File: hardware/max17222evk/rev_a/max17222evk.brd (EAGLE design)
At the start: 160 x 100 mm, 20 parts, among them U1 MAX17222, U2 MAX17222

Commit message: added a first layout for one of the regulators
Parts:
- moved TP6 262.1 mm to (10.2, 25.4)
- moved TP5 236.7 mm to (10.2, 15.2)
- moved TP4 226.6 mm to (10.2, 20.3)
- moved TP3 201.2 mm to (10.2, 10.2)
- moved TP2 180.8 mm to (61.0, 10.2)
- moved TP1 139.8 mm to (53.3, 10.2)
- moved JP2 125.1 mm to (54.6, 19.8), turned to 90 degrees
- moved JP1 122.7 mm to (54.9, 37.3), turned to 90 degrees
- moved L1 87.0 mm to (35.8, 43.8)
- moved S1 84.4 mm to (22.9, 33.0), turned to 90 degrees
- moved S2 79.1 mm to (26.9, 15.2), turned to 90 degrees
- moved L2 77.2 mm to (35.6, 24.6), turned to 180 degrees
- moved R1 74.6 mm to (35.6, 35.1), turned to 90 degrees
- moved R2 63.4 mm to (35.6, 17.5), turned to 90 degrees
- moved C2 62.8 mm to (39.1, 35.1), turned to 270 degrees
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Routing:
- net N$7: track 0.00 -> 12.5 mm
- net IN2: track 0.00 -> 4.37 mm
- net N$12: track 0.00 -> 3.63 mm
- added copper zone on layer 1, net GND
- added copper zone on layer 16, net GND
- added copper zone on layer 1, net IN2
- added copper zone on layer 1, net SW2
- added copper zone on layer 1, net VOUT2

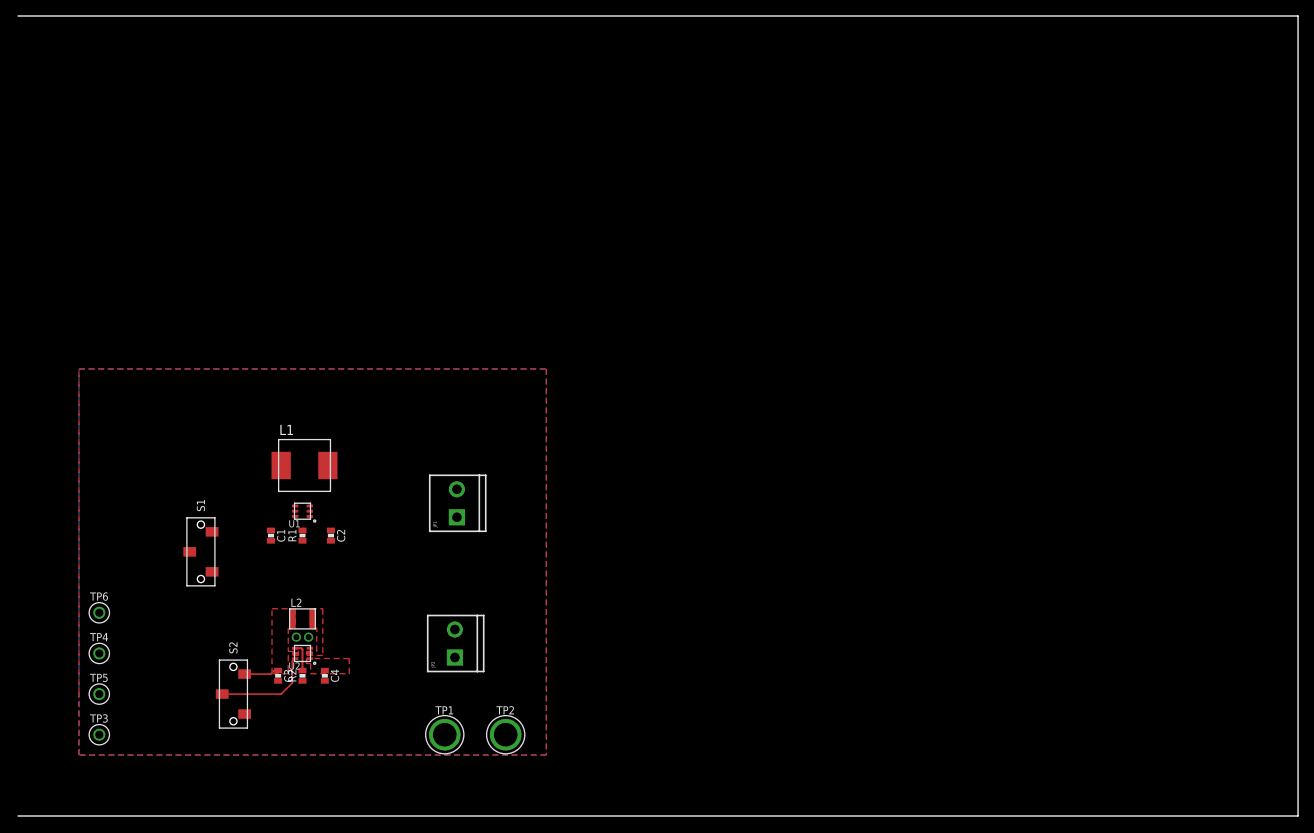
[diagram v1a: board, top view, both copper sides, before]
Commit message: routed board, flipped load screw terminals
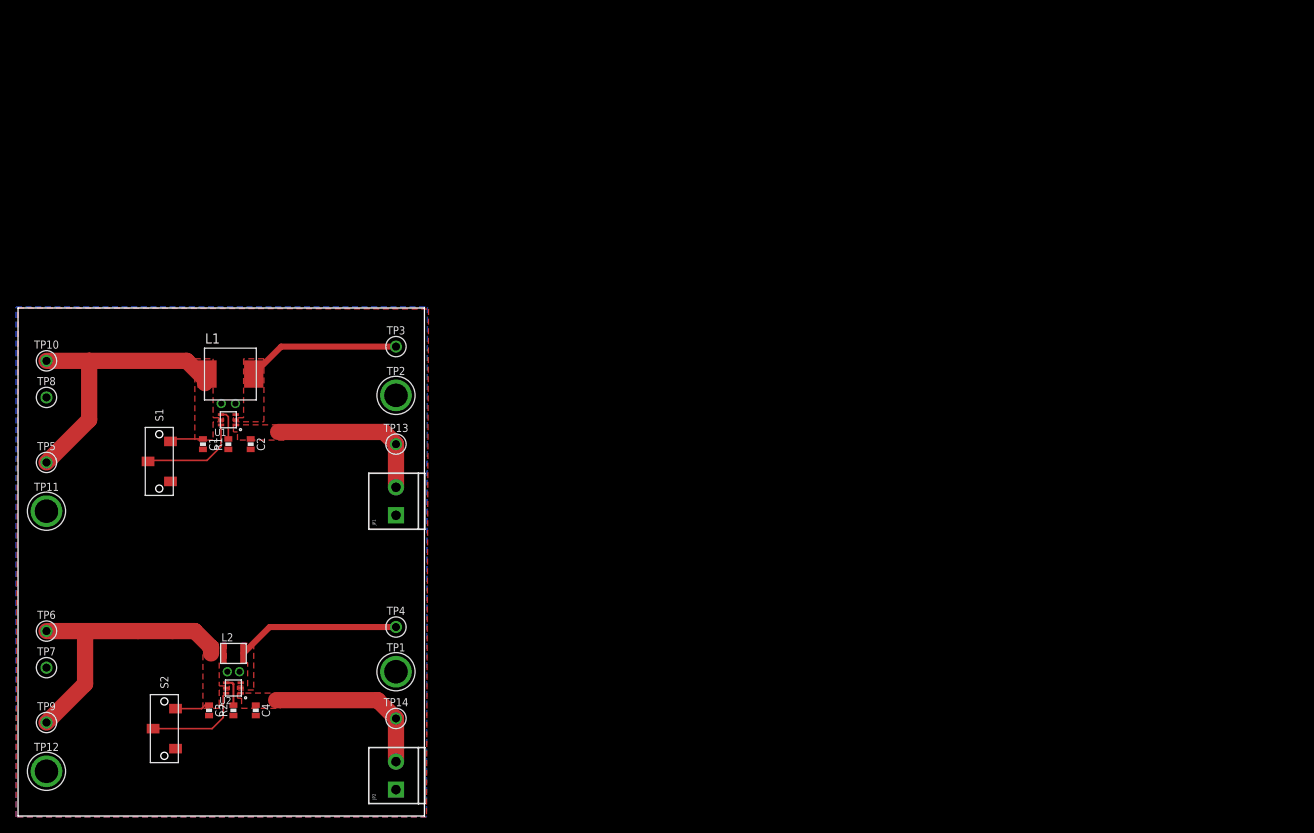
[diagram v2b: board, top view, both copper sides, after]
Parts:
- added TP10, TP13, TP14, TP7, TP8, TP9: TEST_POINT_0.040IN, headers:TESTPOINT_0.040IN
- added TP11, TP12: TEST_POINT_0.112IN, headers:TESTPOINT_0.112IN
- moved TP3 61.1 mm to (47.2, 58.7)
- moved TP2 44.6 mm to (47.2, 52.6)
- moved TP4 37.2 mm to (47.2, 23.6)
- moved TP5 29.7 mm to (3.56, 44.2)
- moved JP2 18.1 mm to (47.2, 3.30)
- moved C2 15.2 mm to (29.1, 46.5)
- moved L1 14.7 mm to (26.5, 55.2)
- moved R1 14.7 mm to (26.3, 46.5)
- moved U1 14.7 mm to (26.3, 49.5)
- moved C1 14.2 mm to (23.1, 46.5)
- moved S1 12.4 mm to (17.7, 44.3)
- moved TP1 9.96 mm to (47.2, 18.0)
- moved L2 9.66 mm to (26.9, 20.3)
- moved U2 9.66 mm to (26.9, 16.0)
- moved R2 9.66 mm to (26.9, 13.2)
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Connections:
- net GND: now also JP1.1, JP2.1, TP11.1, TP12.1, TP7.TESTPOINT, TP8.TESTPOINT; no longer JP1.2, JP2.2
- net IN1: now also TP10.TESTPOINT
- net IN2: now also TP9.TESTPOINT
- net VOUT1: now also JP1.2, TP13.TESTPOINT; no longer JP1.1
- net VOUT2: now also JP2.2, TP14.TESTPOINT; no longer JP2.1
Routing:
- net IN1: track 0.00 -> 40.4 mm
- net IN2: track 4.37 -> 40.0 mm
- net VOUT2: track 0.00 -> 21.3 mm
- net VOUT1: track 0.00 -> 20.8 mm
- net SW2: track 0.00 -> 20.5 mm
- net SW1: track 0.00 -> 19.2 mm
- net N$2: track 0.00 -> 12.6 mm
- net N$5: track 0.00 -> 3.81 mm
- added copper zone on layer 1, net IN1
- added copper zone on layer 1, net SW1
- added copper zone on layer 1, net VOUT1
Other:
- board size 160 x 100 mm -> 50.8 x 63.5 mm

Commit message: layout with silk
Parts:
- added U$1: (no value), logos:UCB_CAL_100MIL
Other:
- board text added: "DISABLE"
- board text added: "ENABLE"
- board text added: "GND"
- board text added: "Inductor Switch"
- board text added: "MAX17222 Evaluation Board Joshua Adkins - Rev A - 07/2017"
- board text added: "Regulator 1 - 3.3V - High Efficiency Inductor"
- board text added: "Regulator 2 - 3.3V - Small Inductor"
- board text added: "VIN"
- board text added: "VOUT"

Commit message: added resistor to enable line
I believe this is necessary for lower power operation.
It is in maxim's EVK
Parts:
- added R3, R4: 33M, passives:0603-RES
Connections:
- removed net N$7: S2.2, U2.6
- new net N$1: R3.2, S1.2
- new net N$3: R4.2, S2.2
- new net N$4: R4.1, U2.6
- net N$2: now also R3.1; no longer S1.2
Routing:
- net N$7: track 12.5 -> 0.00 mm
- net N$4: track 0.00 -> 7.33 mm
- net N$1: track 0.00 -> 6.43 mm
- net N$3: track 0.00 -> 6.36 mm
- net N$2: track 12.6 -> 7.28 mm

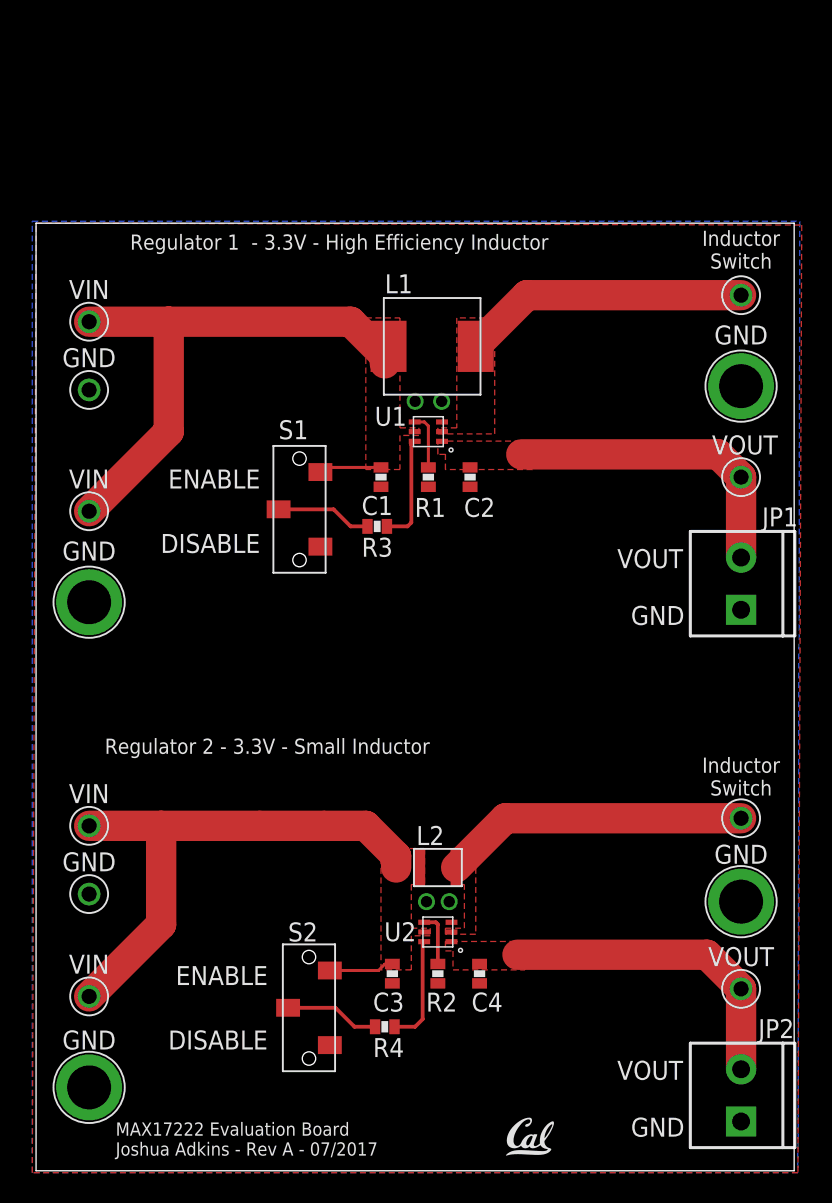
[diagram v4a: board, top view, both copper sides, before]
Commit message: added mounting holes, fixed switch
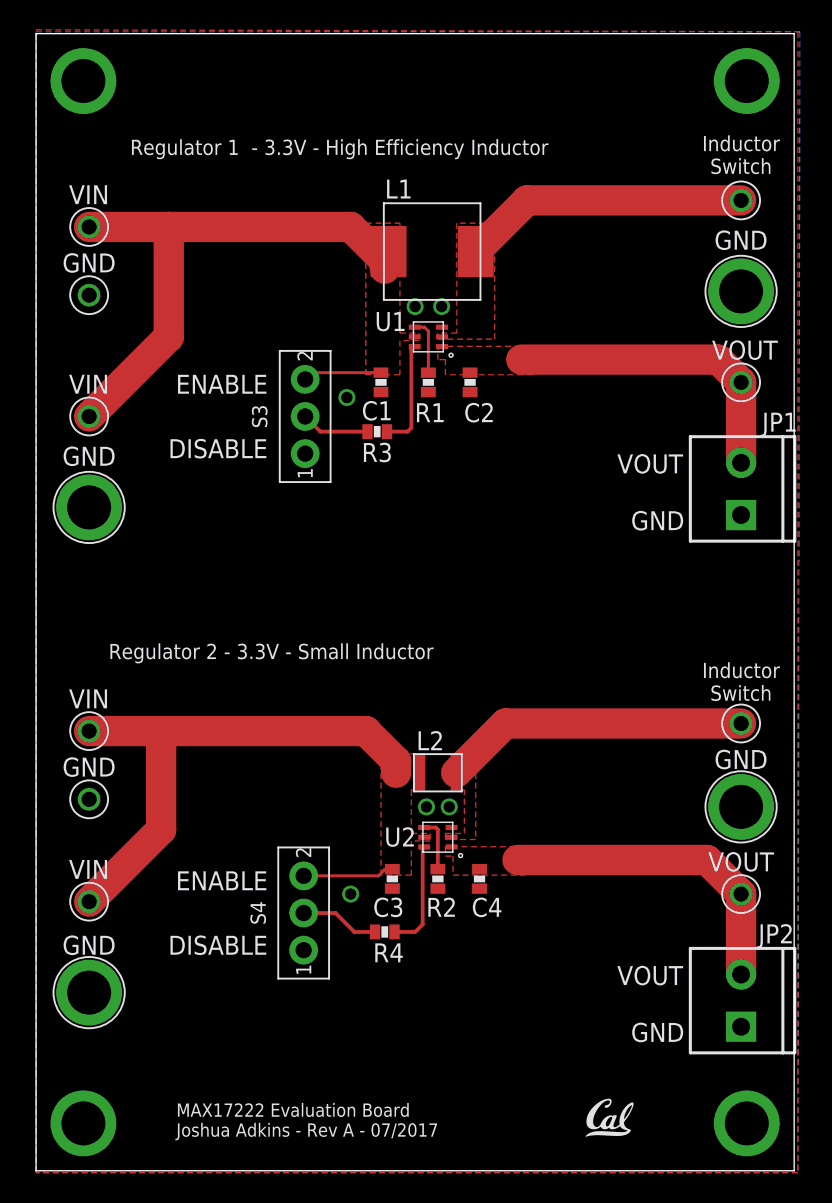
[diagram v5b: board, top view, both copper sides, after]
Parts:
- removed S1, S2: CL-SB-12X, switches:CL-SB-12A
- added S3, S4: TE_SSA12/SPDT, switches:TE_SSA12/SPDT
- moved C1 6.35 mm to (23.1, 52.8)
- moved C2 6.35 mm to (29.1, 52.8)
- moved JP1 6.35 mm to (47.2, 43.9)
- moved L1 6.35 mm to (26.5, 61.6)
- moved L2 6.35 mm to (26.9, 26.7)
- moved R1 6.35 mm to (26.3, 52.8)
- moved R3 6.35 mm to (22.9, 49.5)
- moved TP1 6.35 mm to (47.2, 24.4)
- moved TP10 6.35 mm to (3.56, 63.2)
- moved TP11 6.35 mm to (3.56, 44.5)
- moved TP13 6.35 mm to (47.2, 52.8)
- moved TP14 6.35 mm to (47.2, 18.5)
- moved TP3 6.35 mm to (47.2, 65.0)
- moved TP4 6.35 mm to (47.2, 30.0)
- moved TP5 6.35 mm to (3.56, 50.5)
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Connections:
- net GND: now also S3.1, S4.1; no longer S1.1, S2.1
- net IN1: now also S3.2; no longer S1.3
- net IN2: now also S4.2; no longer S2.3
- net N$1: now also S3.IN; no longer S1.2
- net N$3: now also S4.IN; no longer S2.2
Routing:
- net N$1: track 6.43 -> 4.60 mm
- net IN2: track 40.0 -> 41.7 mm
- net IN1: track 40.4 -> 41.4 mm
- net N$3: track 6.36 -> 5.31 mm
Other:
- board size 50.8 x 63.5 mm -> 50.8 x 76.2 mm

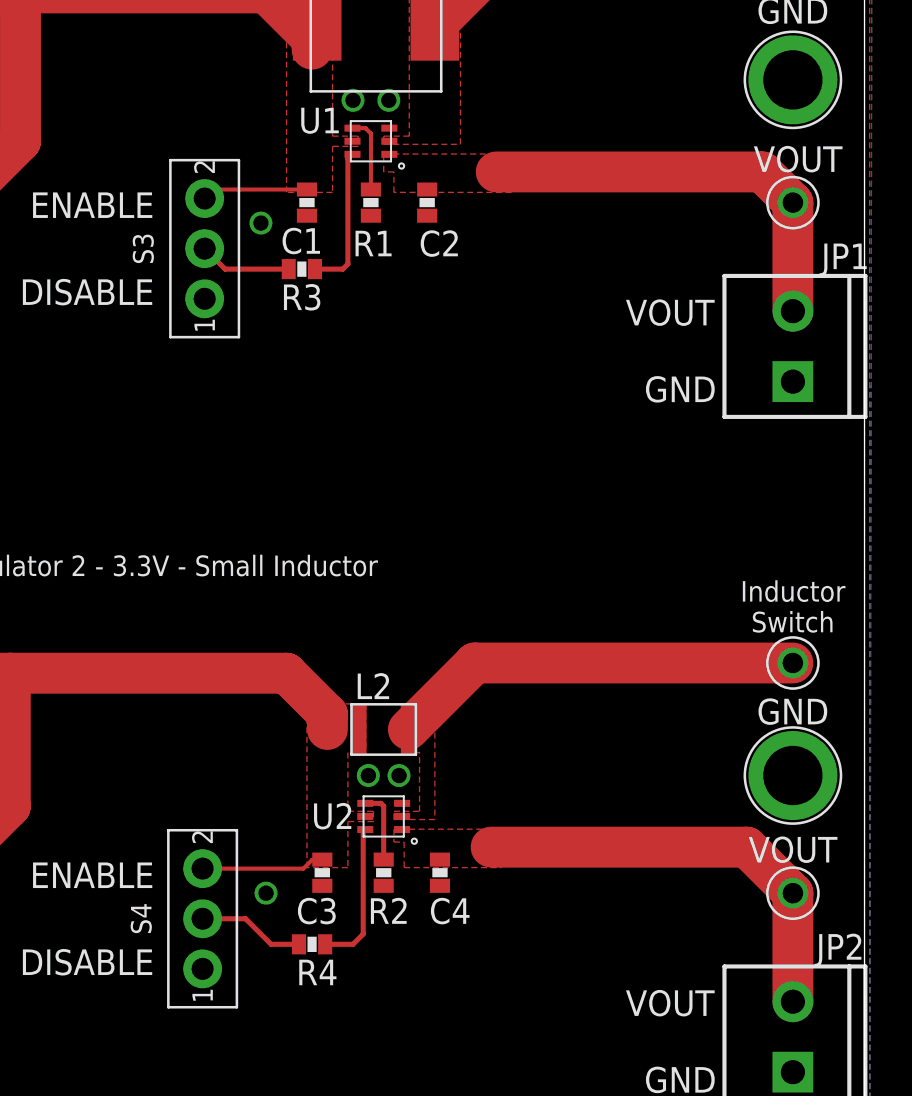
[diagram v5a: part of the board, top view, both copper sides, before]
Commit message: added part numbers and associated BOM
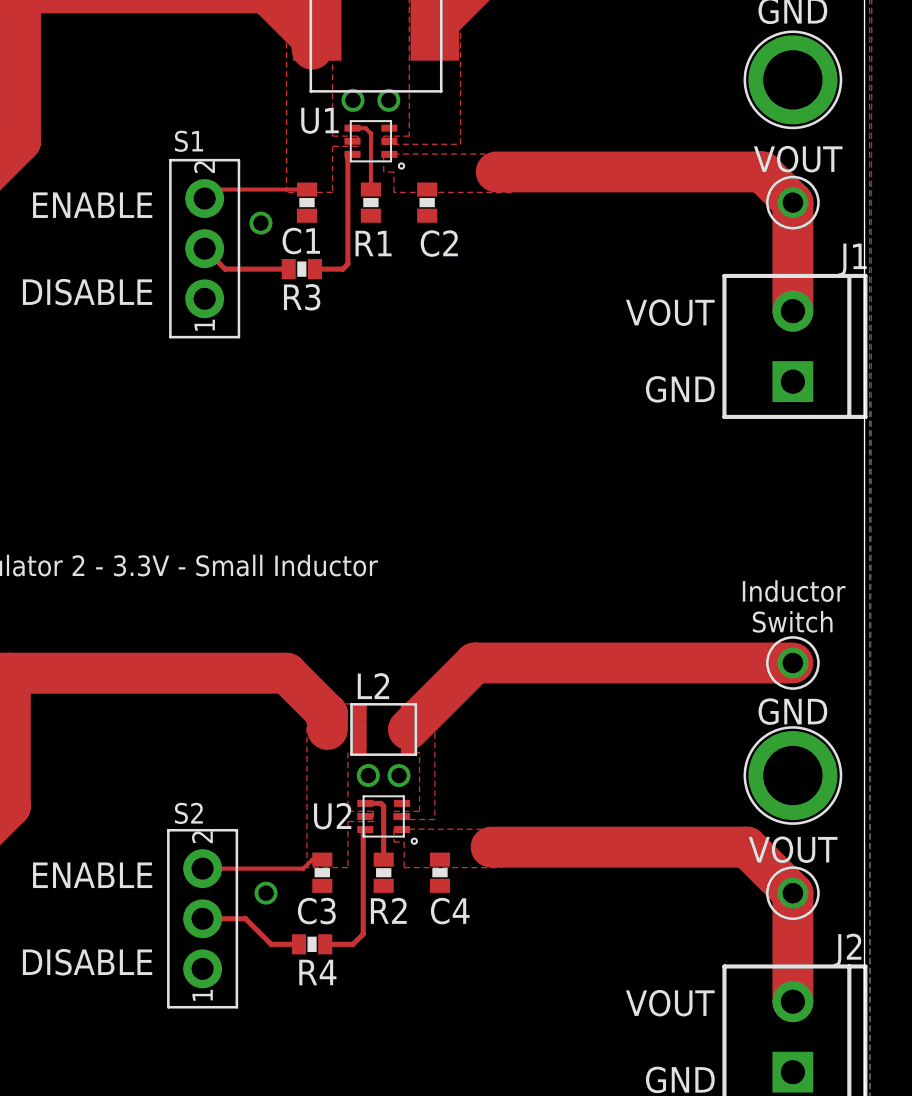
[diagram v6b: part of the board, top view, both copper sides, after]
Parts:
- renumbered JP1 to J1, JP2 to J2, S3 to S1, S4 to S2
